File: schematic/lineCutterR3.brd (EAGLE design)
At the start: 50.8 x 29.2 mm, 60 parts, among them J1 10118192-0001LF, Q1 AO4576, Q2 AO4576, Q4 AO4576, Q5 DMG2305, SW1 KMR2, U1 MS560702BA03-50, U2 MDBT50Q, U3 S25FL128SDPMFIG13S03016, U4 ACS711KEXLT-31AB-T, U6 ICM-20602, X1 2x5 0.05"

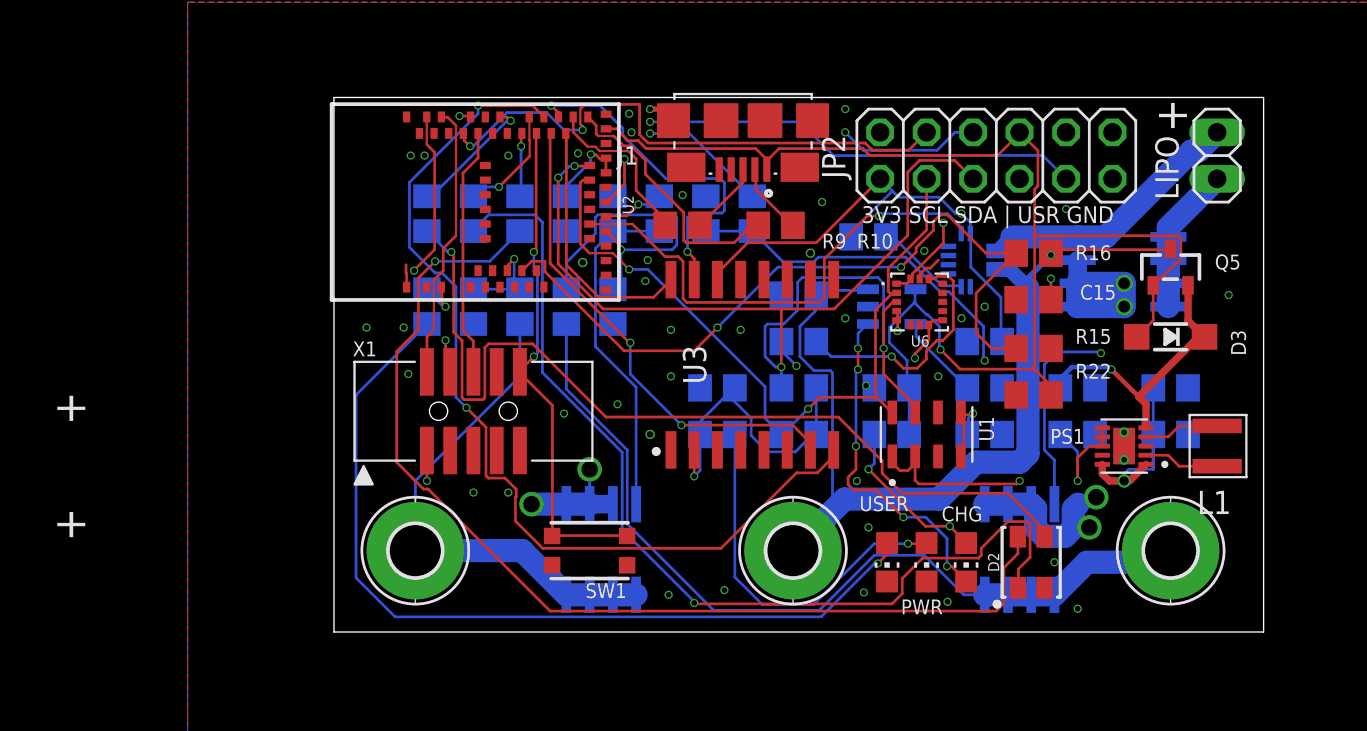
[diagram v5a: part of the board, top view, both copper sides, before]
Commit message: Switch back to 3v3 lin reg
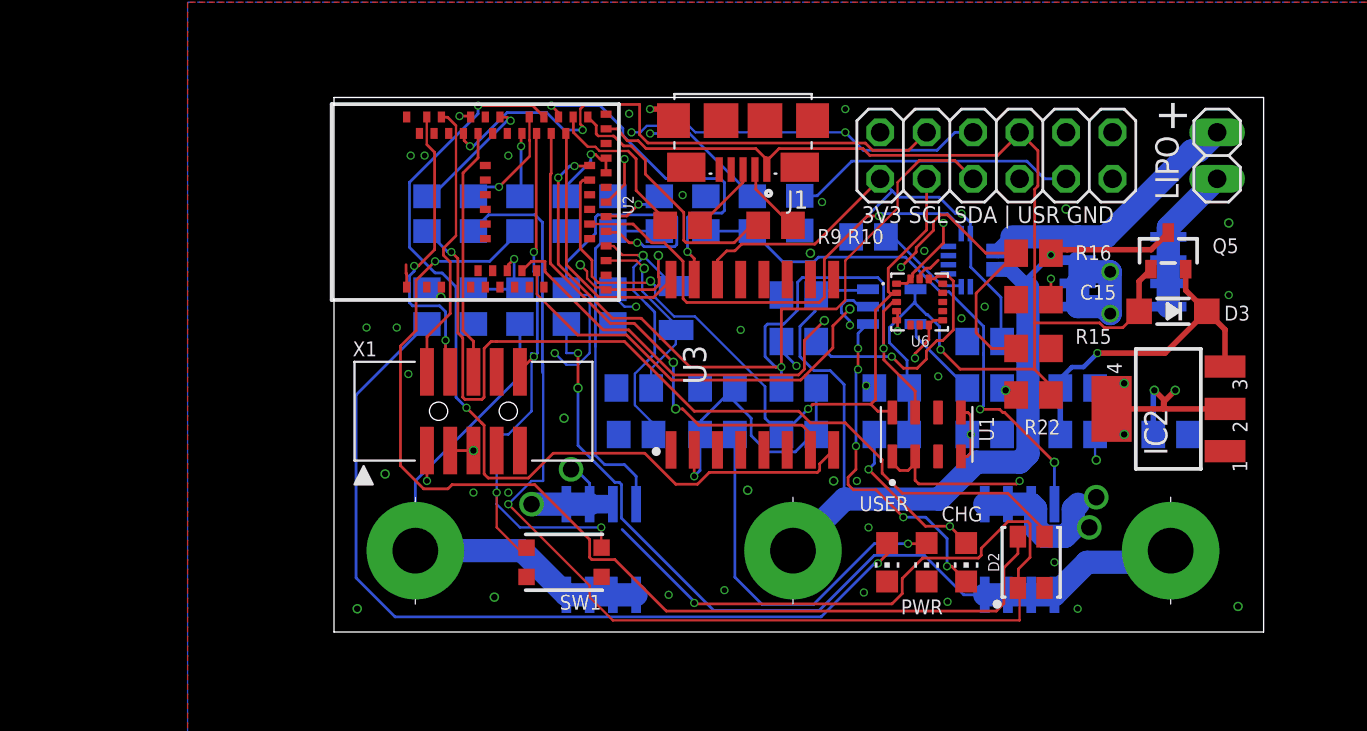
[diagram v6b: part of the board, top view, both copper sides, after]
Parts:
- removed C14: 10u, rcl:C0805
- removed L1: NR3015T1R5N, Line Cutter COTS:NR3015T1R5N
- removed PS1: TPS63031DSKR, Line Cutter COTS:SON50P250X250X80-11N
- added C2, C3: 22pF, rcl:C0805
- added IC2: MC33269ST-3.3T3, linear:SOT223
- added R2: 10k, rcl:R0805
- added Y2: 32.768, adafruit2:XTAL3215
- H3, VCUT_1, VCUT_2: device holes:2,8-PAD -> Line Cutter COTS:2,8-PAD
- moved SW1 1.53 mm to (12.6, 3.81)
- moved D3 1.40 mm to (45.8, 17.5)
- moved Q5 0.90 mm to (45.6, 20.8)
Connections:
- removed net N$18: C11.2, PS1.6, PS1.7, PS1.8
- removed net N$19: L1.2, PS1.4
- removed net N$20: L1.1, PS1.2
- new net N$13: C3.1, U2.17, Y2.P$2
- new net N$2: C2.1, U2.18, Y2.P$1
- new net PHOTO+: JP2.7
- new net PHOTO-: JP2.9, R2.2, U2.13
- net 3.3V: now also IC2.2, IC2.4; no longer C14.2, PS1.1, PS1.10
- net GND: now also C2.2, C3.2, IC2.1, R2.1; no longer C14.1, PS1.11, PS1.3, PS1.9
- net USER: no longer JP2.9
- net VIN_REG1: now also C11.2, IC2.3; no longer PS1.5
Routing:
- net PHOTO-: track 0.00 -> 53.2 mm, vias 0 -> 1
- net USER: track 42.4 -> 1.64 mm, vias 2 -> 1
- net N$21: track 53.4 -> 84.5 mm, vias 1 -> 2
- net N$2: track 0.00 -> 16.1 mm, vias 0 -> 1
- net GND: track 31.9 -> 45.5 mm, vias 48 -> 52
- net CUT_SENSE2: track 17.5 -> 29.4 mm, vias 1 -> 3
- net N$13: track 0.00 -> 10.4 mm, vias 0 -> 1
- net RESET: track 27.4 -> 35.0 mm, vias 2 -> 4
- net N$3: track 37.3 -> 29.8 mm
- net N$18: track 6.89 -> 0.00 mm, vias 1 -> 0
- net VUSB: track 73.3 -> 67.8 mm
- net N$19: track 4.15 -> 0.00 mm
- net N$20: track 4.13 -> 0.00 mm
- net VIN_REG1: track 16.2 -> 19.4 mm
- net MISO: track 51.8 -> 48.9 mm
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
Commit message: Update lineCutterR3.brd
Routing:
- net N$5: track 18.8 -> 17.7 mm
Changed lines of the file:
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@@
 <contactref element="J1" pad="3"/>
 <contactref element="R9" pad="2"/>
-<wire x1="22.352" y1="24.5745" x2="22.352" y2="25.273" width="0.1524" layer="1"/>
-<wire x1="20.0025" y1="22.225" x2="22.352" y2="24.5745" width="0.1524" layer="1"/>
-<wire x1="20.0025" y1="22.225" x2="20" y2="22.225" width="0.1524" layer="1"/>
+<wire x1="22.352" y1="24.0665" x2="22.352" y2="25.273" width="0.1524" layer="1"/>
+<wire x1="20.5105" y1="22.225" x2="22.352" y2="24.0665" width="0.1524" layer="1"/>
+<wire x1="20.5105" y1="22.225" x2="20" y2="22.225" width="0.1524" layer="1"/>
 </signal>
 <signal name="SCL">
@@
 <via x="31.115" y="6.2738" extent="1-16" drill="0.3048"/>
 <via x="28.5244" y="10.16" extent="1-16" drill="0.3048"/>
-<wire x1="28.3751" y1="7.7724" x2="28.0924" y2="8.0551" width="0.1524" layer="1"/>
-<wire x1="28.0924" y1="8.0551" x2="28.0924" y2="8.4549" width="0.1524" layer="1"/>
-<wire x1="31.115" y1="6.2738" x2="29.6164" y2="7.7724" width="0.1524" layer="1"/>
-<wire x1="28.5244" y1="8.8869" x2="28.5244" y2="10.16" width="0.1524" layer="1"/>
-<wire x1="29.6164" y1="7.7724" x2="28.3751" y2="7.7724" width="0.1524" layer="1"/>
-<wire x1="28.0924" y1="8.4549" x2="28.5244" y2="8.8869" width="0.1524" layer="1"/>
+<wire x1="31.115" y1="6.2738" x2="31.115" y2="6.35" width="0.1524" layer="1"/>
+<wire x1="31.115" y1="6.35" x2="28.5244" y2="8.9406" width="0.1524" layer="1"/>
+<wire x1="28.5244" y1="8.9406" x2="28.5244" y2="10.16" width="0.1524" layer="1"/>
 <wire x1="28.5244" y1="10.16" x2="28.5244" y2="14.2369" width="0.1524" layer="16"/>
 <wire x1="28.5244" y1="14.2369" x2="28.6385" y2="14.351" width="0.1524" layer="16"/>
@@
 <wire x1="34.798" y1="11.838" x2="34.798" y2="10.795" width="0.1524" layer="1"/>
 <wire x1="20.955" y1="19.2586" x2="20.955" y2="20.32" width="0.1524" layer="1"/>
-<wire x1="21.9075" y1="20.828" x2="22.2758" y2="21.1963" width="0.1524" layer="1"/>
-<wire x1="20.955" y1="20.32" x2="21.463" y2="20.828" width="0.1524" layer="1"/>
-<wire x1="21.463" y1="20.828" x2="21.9075" y2="20.828" width="0.1524" layer="1"/>
+<wire x1="22.0345" y1="20.955" x2="22.2758" y2="21.1963" width="0.1524" layer="1"/>
+<wire x1="20.955" y1="20.32" x2="21.59" y2="20.955" width="0.1524" layer="1"/>
+<wire x1="21.59" y1="20.955" x2="22.0345" y2="20.955" width="0.1524" layer="1"/>
 <contactref element="IC2" pad="4"/>
 <contactref element="IC2" pad="2"/>
@@
 <wire x1="11.8745" y1="28.7655" x2="12.2555" y2="28.3845" width="0.1524" layer="1"/>
 <wire x1="11.8745" y1="28.7655" x2="14.5415" y2="28.7655" width="0.1524" layer="16"/>
-<wire x1="19.685" y1="20.4089" x2="19.3167" y2="20.7772" width="0.1524" layer="1"/>
-<wire x1="19.685" y1="19.304" x2="19.685" y2="20.4089" width="0.1524" layer="1"/>
+<wire x1="19.685" y1="20.5359" x2="19.4437" y2="20.7772" width="0.1524" layer="1"/>
+<wire x1="19.4437" y1="20.7772" x2="19.3167" y2="20.7772" width="0.1524" layer="1"/>
+<wire x1="19.685" y1="19.304" x2="19.685" y2="20.5359" width="0.1524" layer="1"/>
 <wire x1="12.2555" y1="28.194" x2="12.27" y2="28.145" width="0.1524" layer="1"/>
 <wire x1="19.685" y1="19.304" x2="19.685" y2="19.2586" width="0.1524" layer="1"/>
@@
 <via x="7.874" y="28.7655" extent="1-16" drill="0.3048"/>
 <via x="7.239" y="12.2555" extent="1-16" drill="0.3048"/>
-<wire x1="26.53915" y1="8.84103125" x2="26.42011875" y2="8.722" width="0.1524" layer="1"/>
 <wire x1="8.2032" y1="11.29916875" x2="8.08416875" y2="11.4182" width="0.1524" layer="1"/>
 <wire x1="8.08416875" y1="11.4182" x2="8.0763" y2="11.4182" width="0.1524" layer="1"/>
 <wire x1="8.0763" y1="11.4182" x2="7.239" y2="12.2555" width="0.1524" layer="1"/>
-<wire x1="27.305" y1="9.9514" x2="26.53915" y2="9.18555" width="0.1524" layer="1"/>
-<wire x1="26.53915" y1="9.18555" x2="26.53915" y2="8.84103125" width="0.1524" layer="1"/>
+<wire x1="27.305" y1="9.9514" x2="27.305" y2="9.8244" width="0.1524" layer="1"/>
+<wire x1="27.305" y1="9.8244" x2="27.305" y2="9.4434" width="0.1524" layer="1"/>
+<wire x1="27.305" y1="9.4434" x2="27.305" y2="8.84488125" width="0.1524" layer="1"/>
+<wire x1="27.305" y1="8.84488125" x2="27.18211875" y2="8.722" width="0.1524" layer="1"/>
 <wire x1="16.98368125" y1="9.7682" x2="11.98056875" y2="9.7682" width="0.1524" layer="1"/>
 <wire x1="11.98056875" y1="9.7682" x2="10.62416875" y2="8.4118" width="0.1524" layer="1"/>
 <wire x1="8.42583125" y1="8.4118" x2="8.2032" y2="8.63443125" width="0.1524" layer="1"/>
 <wire x1="8.2032" y1="8.63443125" x2="8.2032" y2="11.29916875" width="0.1524" layer="1"/>
-<wire x1="26.42011875" y1="8.722" x2="20.5086625" y2="8.722" width="0.1524" layer="1"/>
+<wire x1="27.18211875" y1="8.722" x2="20.5086625" y2="8.722" width="0.1524" layer="1"/>
 <wire x1="20.5086625" y1="8.722" x2="19.8638625" y2="8.0772" width="0.1524" layer="1"/>
 <wire x1="10.62416875" y1="8.4118" x2="8.42583125" y2="8.4118" width="0.1524" layer="1"/>

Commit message: Final board stuff
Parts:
- U4: value ACS711KEXLT-31AB-T -> ACS711KEXLT-15AB-T
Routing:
- net N$21: track 84.5 -> 53.3 mm, vias 2 -> 1
- net SDA: track 64.0 -> 62.8 mm
- net CUT2: track 11.8 -> 12.7 mm
- net N$4: track 4.69 -> 5.45 mm
- net N$1: track 9.75 -> 9.06 mm
- net GND: track 45.5 -> 44.9 mm, vias 52 -> 57
- net RESET: track 35.0 -> 34.4 mm
- net BATT_SENSE: track 43.8 -> 43.2 mm
